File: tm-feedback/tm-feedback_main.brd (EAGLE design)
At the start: 100 x 80 mm, 36 parts

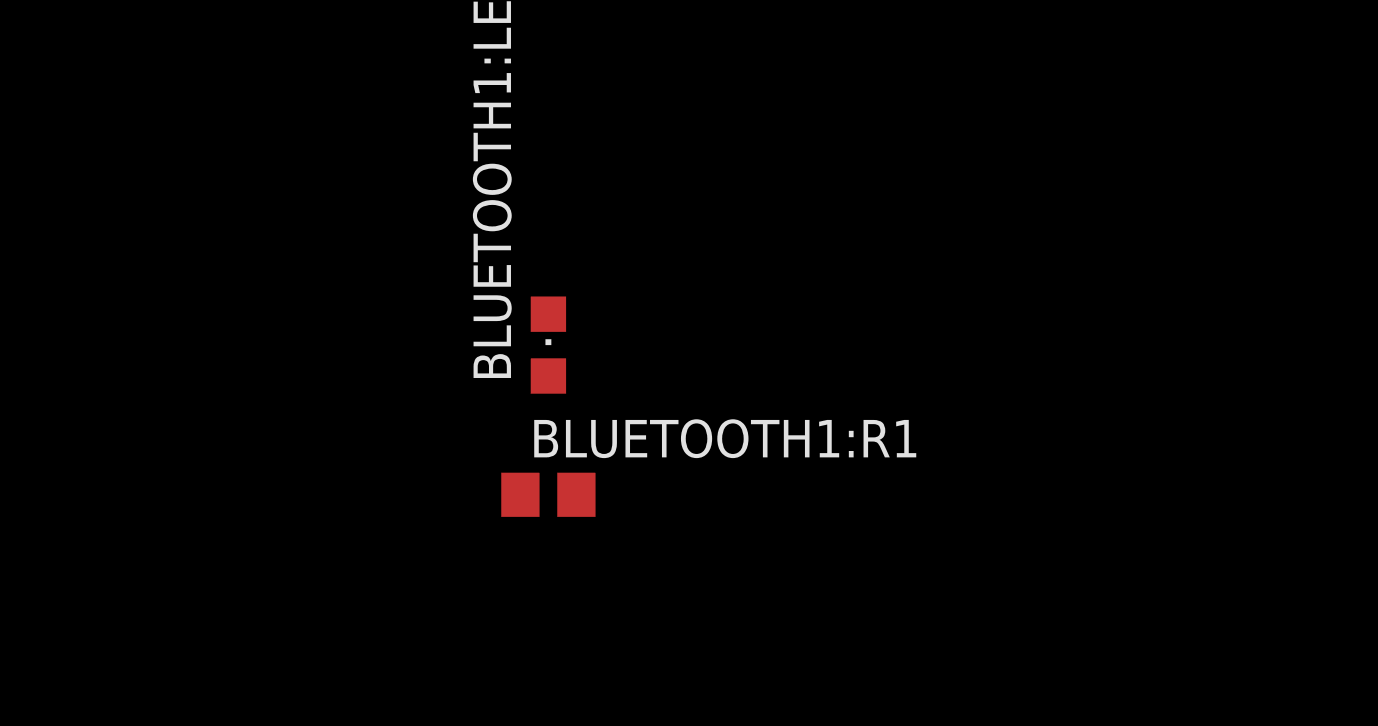
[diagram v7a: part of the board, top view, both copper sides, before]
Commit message: Added dsPIC into microcontroller schematic
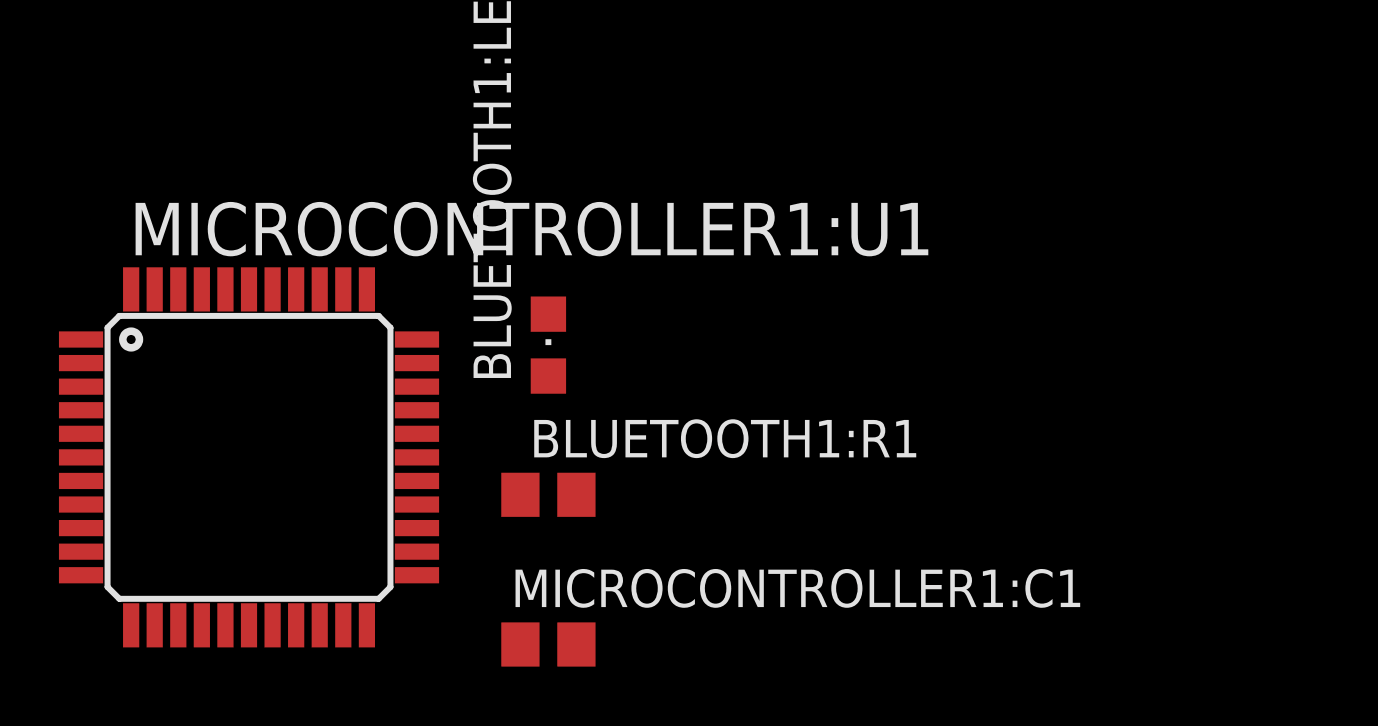
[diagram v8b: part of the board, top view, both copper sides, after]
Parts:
- added MICROCONTROLLER1:C1: (no value), rcl:C0805
- added MICROCONTROLLER1:U1: DSPIC33EP512MC504, tactile-music:TQFP44
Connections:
- new net MICROCONTROLLER1:AVDD: MICROCONTROLLER1:U1.17
- new net MICROCONTROLLER1:AVSS: MICROCONTROLLER1:U1.16
- new net MICROCONTROLLER1:VSS: MICROCONTROLLER1:U1.6
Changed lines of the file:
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@@
 <layer number="48" name="Document" color="7" fill="1" visible="yes" active="yes"/>
 <layer number="49" name="Reference" color="7" fill="1" visible="yes" active="yes"/>
+<layer number="50" name="dxf" color="7" fill="1" visible="no" active="no"/>
 <layer number="51" name="tDocu" color="7" fill="1" visible="yes" active="yes"/>
 <layer number="52" name="bDocu" color="7" fill="1" visible="yes" active="yes"/>
@@
 <element name="BLUETOOTH1:R1" library="resistor" package="R0805" value="" x="-77.47" y="-234.95"/>
 <element name="BLUETOOTH1:LED1" library="led" package="CHIPLED_0805" value="" x="-77.47" y="-229.87"/>
+<element name="MICROCONTROLLER1:C1" library="rcl" package="C0805" value="" x="-77.47" y="-240.03"/>
+<element name="MICROCONTROLLER1:U1" library="tactile-music" package="TQFP44" value="DSPIC33EP512MC504" x="-87.63" y="-233.68"/>
 </elements>
 <signals>
@@
 <contactref element="BLUETOOTH1:U$1" pad="15"/>
 </signal>
+<signal name="MICROCONTROLLER1:VSS">
+<contactref element="MICROCONTROLLER1:U1" pad="6"/>
+</signal>
+<signal name="MICROCONTROLLER1:AVSS">
+<contactref element="MICROCONTROLLER1:U1" pad="16"/>
+</signal>
+<signal name="MICROCONTROLLER1:AVDD">
+<contactref element="MICROCONTROLLER1:U1" pad="17"/>
+</signal>
 </signals>
